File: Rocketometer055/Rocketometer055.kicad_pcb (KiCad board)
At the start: 2 copper layers, 55.9 x 22.9 mm, 60 parts, among them J102 Micro_SD_Card_Det_Hirose_DM3AT, J601 USB_MICROB, J801 JST 2mm, Q650 PMOS, U101 LPC2148, U201 BME280, U301 BNO085, U401 ADXL375, U501 FGPMMOPA6H, U501 MPU9250, U701 3.3V, U801 MCP73831, X511 uFL, Y101 12MHz, Y301 32kiHz

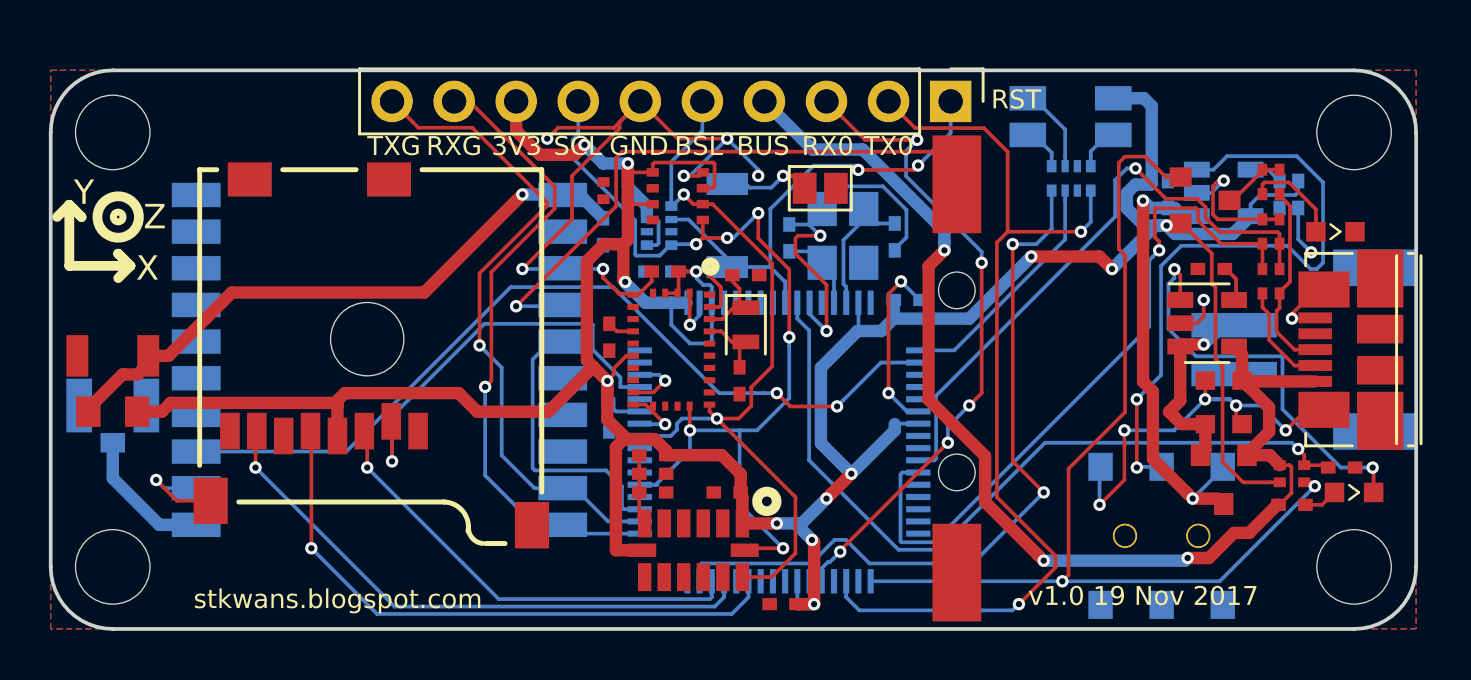
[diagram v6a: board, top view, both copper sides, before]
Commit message: Finished baseline routing of second version of Rocketometer055
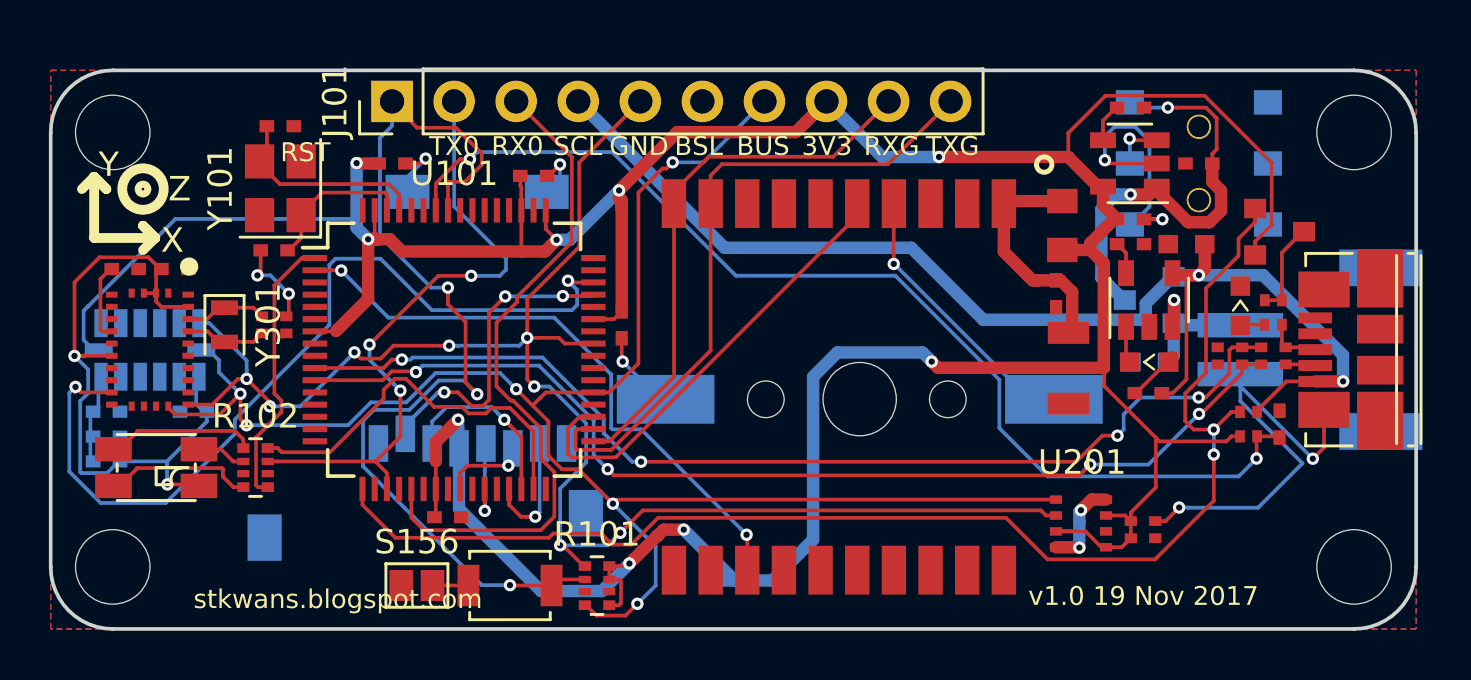
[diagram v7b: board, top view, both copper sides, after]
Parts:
- removed C327: 22pF, KwanSystems:SMD_0402
- removed X511: uFL, KwanSystems:U.FL
- B504, C401, C405, C406, C803, D802, J102, R406, U401: moved to B.Cu
- C143, C151, C161, C162, C163, C501, C704, C714, C715, R101, R102, S157, U101, U501, U701, Y101: moved to F.Cu
- C326: footprint KwanSystems:SMD_0402 -> KwanSystems:R_Array_Convex_2x0402
- D101: footprint HSMF-C118 -> KwanSystems:HSMF-C118; moved to F.Cu
- U599: renamed from U501; value MPU9250 -> FGPMMOPA6H
- moved D101 40.1 mm to (131.3, 95.0)
- moved L501 39.6 mm to (168.4, 85.1), turned to 90 degrees
- moved C503 39.1 mm to (168.7, 90.9), turned to 90 degrees
- moved R102 35.4 mm to (135.4, 95.0), turned to 0 degrees
- moved C206 25.7 mm to (171.7, 97.5), turned to 0 degrees
- moved C162 25.4 mm to (136.1, 86.1), turned to 0 degrees
- moved U401 23.7 mm to (131.1, 90.2)
- moved S156 23.2 mm to (142.0, 99.8), turned to 90 degrees
- moved Y101 23.1 mm to (136.4, 83.6), turned to 90 degrees
- moved J101 22.9 mm to (141.0, 80.0), turned to 90 degrees
- moved C405 22.6 mm to (129.3, 92.7)
- moved C406 22.4 mm to (129.3, 93.7)
- moved R406 22.4 mm to (129.3, 94.7)
- moved C401 22.1 mm to (132.8, 92.7)
- moved C163 21.8 mm to (141.0, 82.5)
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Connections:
- C326 pad 1: GND -> /BNO055/XIN32
- J102 pad 1: Net-(J102-Pad1) -> (no net)
- J102 pad 8: Net-(J102-Pad8) -> (no net)
- J601 pad 4: Net-(J601-Pad4) -> (no net)
- R102 pad 2: /DB -> /DR
- R102 pad 4: /DR -> /DB
- R102 pad 5: /TX0(PWMR) -> /PWMB
- R102 pad 7: /PWMB -> /TX0(PWMR)
- R651 pad 1: /VBUS -> VCC
- R651 pad 2: VCC -> /USB_ON
- R651 pad 3: /USB_SOFTCONNECT -> /VBUS
- R651 pad 4: /USB_ON -> /USB_SOFTCONNECT
- U101 pad 12: Net-(U101-Pad12) -> (no net)
- U101 pad 13: Net-(U101-Pad13) -> (no net)
- U101 pad 14: Net-(U101-Pad14) -> (no net)
- U101 pad 15: Net-(U101-Pad15) -> (no net)
- U101 pad 16: Net-(U101-Pad16) -> (no net)
- U101 pad 20: Net-(U101-Pad20) -> (no net)
- U101 pad 22: Net-(U101-Pad22) -> (no net)
- U101 pad 24: Net-(U101-Pad24) -> (no net)
- U101 pad 26: Net-(U101-Pad26) -> (no net)
- U101 pad 28: Net-(U101-Pad28) -> (no net)
- U101 pad 3: Net-(U101-Pad3) -> (no net)
- U101 pad 32: Net-(U101-Pad32) -> (no net)
- U101 pad 36: Net-(U101-Pad36) -> (no net)
- U101 pad 38: Net-(U101-Pad38) -> (no net)
- U101 pad 39: Net-(U101-Pad39) -> (no net)
- U101 pad 4: Net-(U101-Pad4) -> (no net)
- U101 pad 40: Net-(U101-Pad40) -> (no net)
- U101 pad 44: Net-(U101-Pad44) -> (no net)
- U101 pad 47: Net-(U101-Pad47) -> (no net)
- U101 pad 48: Net-(U101-Pad48) -> (no net)
- U101 pad 5: Net-(U101-Pad5) -> (no net)
- U101 pad 52: Net-(U101-Pad52) -> (no net)
- U101 pad 53: Net-(U101-Pad53) -> (no net)
- U101 pad 54: Net-(U101-Pad54) -> (no net)
- U101 pad 55: Net-(U101-Pad55) -> (no net)
- U101 pad 56: Net-(U101-Pad56) -> (no net)
- U101 pad 60: Net-(U101-Pad60) -> (no net)
- U101 pad 64: Net-(U101-Pad64) -> (no net)
- U101 pad 8: Net-(U101-Pad8) -> (no net)
- U101 pad 9: Net-(U101-Pad9) -> (no net)
- U301 pad 7: Net-(U301-Pad7) -> (no net)
- U301 pad 8: Net-(U301-Pad8) -> (no net)
- U401 pad 8: /HighAcc/INT -> (no net)
- U501 pad 11: /GPS/ANT -> (no net)
- U501 pad 14: Net-(U501-Pad14) -> (no net)
- U501 pad 2: Net-(U501-Pad2) -> (no net)
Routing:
- net GND: track 90.8 -> 49.2 mm, vias 22 -> 12
- net VCC: track 155.2 -> 192.2 mm, vias 13 -> 11
- net /SDA(BSL): track 31.8 -> 66.6 mm, vias 2 -> 8
- net /ACCINT: track 2.65 -> 35.6 mm, vias 1 -> 2
- net /SCL: track 38.7 -> 71.0 mm
- net /Regulator/PWR_EN: track 26.3 -> 2.16 mm, vias 2 -> 1
- net /RST: track 19.1 -> 40.8 mm, vias 2 -> 3
- net /SCK0: track 24.7 -> 3.67 mm
- net /USBD+: track 24.9 -> 43.9 mm, vias 1 -> 4
- net /MISO0: track 23.9 -> 4.99 mm
- net /GPS/VGPS: track 25.5 -> 9.62 mm, vias 1 -> 0
- net /Charger/STAT-: track 16.9 -> 1.71 mm, vias 2 -> 0
- net /USBD-: track 28.7 -> 43.8 mm, vias 1 -> 4
- net /PWMG: track 30.9 -> 15.8 mm, vias 2 -> 0
- net /GPS/VBACKUP: track 24.5 -> 11.3 mm
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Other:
- board text removed: "D"

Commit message: Working on Rocketometer055
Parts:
- removed B504: Coin_Cell, KwanSystems:CR1220-2
- removed C123, C406, C704: 1uF, KwanSystems:SMD_0402
- removed C143, C151, C163, C401, C501, C714: 100nF, KwanSystems:SMD_0402
- removed C161, C162: 33pF, KwanSystems:SMD_0402
- removed C206: 100nF, KwanSystems:R_Array_Convex_2x0402
- removed C303, C309: 0.1uF, KwanSystems:SMD_0402
- removed C326, C623: 22pF, KwanSystems:R_Array_Convex_2x0402
- removed C503: 10uF, KwanSystems:SMD_1206
- removed C715: 4.7nF, KwanSystems:SMD_0402
- removed C802, C803: 4.7uF, KwanSystems:SMD_0603
- removed D101: HSMF-C118, KwanSystems:HSMF-C118
- removed D650: BLUE, KwanSystems:D_0603
- removed D801: YELLOW, KwanSystems:D_0603
- removed D802: DCC, KwanSystems:SOT-23
- removed J101: ~, Pin_Headers:Pin_Header_Straight_1x10_Pitch2.54mm
- removed J102: Micro_SD_Card_Det_Hirose_DM3AT, KwanSystems:MICROSD-SOCKET-PP
- removed J601: USB_MICROB, KwanSystems:USB_Micro-B_Molex_47346-0001
- removed J801: JST 2mm, KwanSystems:SPARKFUN_JST_POWER
- removed L501: Ferrite, KwanSystems:SMD_0805
- removed Q650: PMOS, KwanSystems:SOT-23
- removed R101: 10k, KwanSystems:R_Array_Convex_4x0402
- removed R102: 1.5k, KwanSystems:R_Array_Convex_4x0402
- removed R406: 100, KwanSystems:SMD_0402
- removed R611: 22k, KwanSystems:SMD_0402
- removed R623: 33, KwanSystems:R_Array_Convex_2x0402
- removed R650: 1.5k, KwanSystems:R_Array_Convex_2x0402
- removed R651: 10k, KwanSystems:R_Array_Convex_2x0402
- removed R801: 10k, KwanSystems:SMD_0402
- removed R804: 1.5k, KwanSystems:SMD_0402
- removed S156: SOLDERJUMPERNO, Connectors:GS2
- removed S157: SPST, KwanSystems:SW_SPST_B3U-1000P
- removed S701: SPDT, KwanSystems:SWITCH_DPDT_AZY0202
- removed U101: LPC2148, Housings_QFP:LQFP-64_10x10mm_Pitch0.5mm
- removed U501: FGPMMOPA6H, KwanSystems:FGPMMOPA6H
- removed U599: FGPMMOPA6H, KwanSystems:Axis
- removed U701: 3.3V, TO_SOT_Packages_SMD:SOT-23-5
- removed U801: MCP73831, TO_SOT_Packages_SMD:SOT-23-5
- removed Y101: 12MHz, Crystals:Crystal_SMD_Abracon_ABM8G-4pin_3.2x2.5mm
- removed Y301: 32kiHz, Crystals:Crystal_SMD_2012-2pin_2.0x1.2mm
- added C010: 1uF, KwanSystems:SMD_0402, B.Cu at (176.0, 86.9)
- added C020: 22pF, KwanSystems:SMD_0402, B.Cu at (176.0, 90.7)
- added C030: 22pF, KwanSystems:SMD_0402, B.Cu at (176.0, 94.5)
- added C204: 1uF, KwanSystems:SMD_0402, B.Cu at (173.5, 99.1)
- added C214: 100nF, KwanSystems:SMD_0402, B.Cu at (172.2, 99.1)
- added C215: 4.7nF, KwanSystems:SMD_0402, B.Cu at (167.6, 99.1)
- added C301: 4.7uF, KwanSystems:SMD_0402, B.Cu at (171.2, 85.3)
- added C302: 4.7uF, KwanSystems:SMD_0402, B.Cu at (171.2, 84.1)
- added C403: 18pF, KwanSystems:SMD_0402, F.Cu at (167.9, 96.5)
- added C423: 1uF, KwanSystems:SMD_0402, F.Cu at (160.3, 83.3)
- added C443: 100nF, KwanSystems:SMD_0402, F.Cu at (152.7, 91.4)
- added C449: 100nF, KwanSystems:SMD_0402, F.Cu at (156.2, 99.3)
- added C451: 100nF, KwanSystems:SMD_0402, F.Cu at (157.9, 99.3)
- added C461: 33pF, KwanSystems:SMD_0402, F.Cu at (160.3, 99.3)
- added C462: 33pF, KwanSystems:SMD_0402, F.Cu at (164.8, 99.3)
- added C463: 100nF, KwanSystems:SMD_0402, F.Cu at (166.4, 96.5)
- added C907: 100nF, KwanSystems:SMD_0402, F.Cu at (142.2, 95.2)
- added C908: 10uF, 0603-CAP, F.Cu at (142.2, 94.0)
- added D050: BLUE, LED-0603, B.Cu at (176.0, 81.0)
- added D301: YELLOW, LED-0603, B.Cu at (167.6, 80.0)
- added D302: DCC, KwanSystems:SOT-23, B.Cu at (171.2, 87.6)
- added D401: HSMF-C118, HSMF-C118, B.Cu at (140.5, 81.8)
- added J001: USB_MICROB, UB-MC5BR3-SD204-4S, B.Cu at (181.4, 90.2)
- added J301: JST 2mm, JST-2-SMD, F.Cu at (179.6, 90.2)
- added J401: M07, 1X08, F.Cu at (163.8, 80.0)
- added J701: Micro_SD_Card_Det_Hirose_DM3AT, MICROSD-SOCKET-PP, B.Cu at (163.3, 83.6)
- added JP3: STAND-OFFTIGHT, STAND-OFF-TIGHT, F.Cu at (142.2, 90.2)
- added Q050: PMOS, KwanSystems:SOT-23, F.Cu at (176.0, 82.0)
- added R010: 10k, 0402-RES, B.Cu at (176.0, 85.6)
- added R011: 100k, 0402-RES, B.Cu at (176.0, 88.1)
- added R020: 33, 0402-RES, B.Cu at (176.0, 89.4)
- added R030: 33, 0402-RES, B.Cu at (176.0, 91.9)
- added R031: 1.5k, 0402-RES, B.Cu at (176.0, 93.2)
- added R050: 1.5k, 0402-RES, B.Cu at (176.0, 83.1)
- added R051: 10k, 0402-RES, F.Cu at (176.0, 84.6)
- added R301: 10k, 0402-RES, B.Cu at (168.4, 81.8)
- added R302: 1.5k, 0402-RES, B.Cu at (166.9, 81.8)
- added R401: 10k, CRA04, F.Cu at (149.9, 83.6)
- added S201: SPDT, AYZ0202, B.Cu at (169.7, 93.2)
- added S456: SOLDERJUMPERNO, SJ_2S-NO, B.Cu at (147.6, 95.8)
- added S457: SPST, B3U-1000P, B.Cu at (147.6, 92.5)
- added S458: B3U-1000P, B3U-1000P, B.Cu at (147.6, 87.4)
- added U$1: , KWAN_ACC, F.Cu at (134.6, 90.2)
- added U$4: , AXES, F.Cu at (128.3, 94.0)
- added U$5: , KWAN_ACC, B.Cu at (134.6, 90.2)
- added U$6: , OSHW_ACC, B.Cu at (135.9, 98.0)
- added U902: AD7991, SOT-23-8, F.Cu at (142.5, 98.0)
- added Y401: 12MHz, CRYSTAL_SMD_2MM_2_5MM, F.Cu at (162.6, 99.3)
- added Y402: 32kiHz, ABS06, F.Cu at (167.9, 93.2)
- C405: value 100nF -> 18pF; moved to F.Cu
- U201: value BME280 -> 3.3V; footprint KwanSystems:BME280 -> SOT-23-5; moved to B.Cu
- U301: value BNO085 -> MCP73831; footprint KwanSystems:BNO055 -> SOT-23-5; moved to B.Cu
- U401: value ADXL375 -> LPC2148; footprint KwanSystems:ADXL375 -> Housings_QFP:LQFP-64_10x10mm_Pitch0.5mm; moved to F.Cu
- moved U301 41.0 mm to (171.2, 81.8), turned to 270 degrees
- moved C405 38.7 mm to (167.9, 90.7), turned to 270 degrees
- moved U401 29.2 mm to (160.3, 90.9), turned to 180 degrees
- moved U201 1.93 mm to (169.9, 99.1), turned to 0 degrees
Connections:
- C405 pad 1: /HighAcc/VS -> GND
- C405 pad 2: GND -> /RTXC2
- U201 pad 1: GND -> /VIN+
- U201 pad 2: VCC -> GND
- U201 pad 3: /SDA(BSL) -> /PWR_EN
- U201 pad 4: /SCL -> /BYP
- U201 pad 5: GND -> VCC
- U301 pad 1: (no net) -> /N$4
- U301 pad 3: VCC -> /VLIPO
- U301 pad 4: VCC -> /VBUS
- U301 pad 5: GND -> /N$2
- U401 pad 1: VCC -> Net-(U401-Pad1)
- U401 pad 10: (no net) -> /USBD+
- U401 pad 11: (no net) -> /USBD-
- U401 pad 12: GND -> Net-(U401-Pad12)
- U401 pad 13: /SDA(BSL) -> Net-(U401-Pad13)
- U401 pad 14: /SCL -> Net-(U401-Pad14)
- U401 pad 2: GND -> Net-(U401-Pad2)
- U401 pad 3: (no net) -> /RTXC1
- U401 pad 4: GND -> Net-(U401-Pad4)
- U401 pad 5: GND -> /RTXC2
- U401 pad 6: /HighAcc/VS -> GND
- U401 pad 8: (no net) -> Net-(U401-Pad8)
- U401 pad 9: (no net) -> Net-(U401-Pad9)
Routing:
- net VCC: track 192.2 -> 0.00 mm, vias 11 -> 0
- net /SCL: track 71.0 -> 0.00 mm, vias 6 -> 0
- net /SDA(BSL): track 66.6 -> 0.00 mm, vias 8 -> 0
- net /VLIPO: track 0.00 -> 57.1 mm, vias 0 -> 6
- net /USB_SOFTCONNECT: track 53.9 -> 0.00 mm, vias 2 -> 0
- net GND: track 49.2 -> 0.00 mm, vias 12 -> 0
- net /ACCINT: track 35.6 -> 0.00 mm, vias 2 -> 0
- net /USBD+: track 43.9 -> 14.8 mm, vias 4 -> 1
- net /USBD-: track 43.8 -> 14.7 mm, vias 4 -> 1
- net /GPS_TX: track 27.0 -> 0.00 mm
- net /N$6: track 0.00 -> 26.4 mm, vias 0 -> 1
- net /TX0(PWMR): track 26.1 -> 0.00 mm, vias 3 -> 0
- net /PPS: track 24.9 -> 0.00 mm, vias 2 -> 0
- net /GPS_RX: track 22.3 -> 0.00 mm
- net /RX0: track 27.7 -> 7.12 mm
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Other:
- board text added: "+"
- board text added: "-"
- board text added: "Acc/Gyro"
- board text added: "Baro"
- board text added: "Boot"
- board text added: "Compass"
- board text added: "D"
- board text added: "HighAcc"
- board text added: "Reset"
- board text added: "RocketometerMPU6050"
- board text added: "SDA"
- board text added: "St Kwan's Home for"
- board text added: "VBUS"
- board text added: "a division of"
- board text added: "the Terminally ADD"
- board text added: "v1.0 19 Nov 2012"
- board text removed: "BUS"
- board text removed: "RST"
- board text removed: "RXG"
- board text removed: "RocketometerBNO055"
- board text removed: "TXG"
- board text removed: "v1.0 19 Nov 2017"
